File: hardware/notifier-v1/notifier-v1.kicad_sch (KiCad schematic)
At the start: 32 parts, among them J1 USB-C, J2 GC9A01, SW1 RESET, SW2 BOOT, SW3 BUTTON, U1 ESP32-S3-WROOM-1-N8R2, U2 USBLC6-2SC6, U3 AMS1117-3.3, U4 BME688

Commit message: hardware: notifier-v1 rev after design review (buck, sensor peninsula, no via-in-pad)
Review findings applied: TLV62569 buck instead of AMS1117 (0.6 W into the sensor), 500 mA
polyfuse, BME688 on a peninsula with the neck away from the module, custom DRC rule and
KRT settings against vias in SMD pads, signals on the outer layers only, display socket
face past the edge with pin names, more debug pads, antenna strip without pours/vias.
Safe cleanup of router leftovers, one-command pipeline, order checklist.

Co-Authored-By: Claude Opus 5.5 <noreply@anthropic.com>
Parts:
- removed U3: AMS1117-3.3, Package_TO_SOT_SMD:SOT-223-3_TabPin2, symbol Regulator_Linear:AMS1117-3.3
- added F1: 500mA, Fuse:Fuse_1206_3216Metric, symbol Device:Polyfuse
- added L1: 2.2u, Inductor_SMD:L_Cenker_CKCS4030, symbol Device:L
- added R10: 22k, Resistor_SMD:R_0402_1005Metric, symbol Device:R
- added R9: 100k, Resistor_SMD:R_0402_1005Metric, symbol Device:R
- added TP4: 3V3, TestPoint:TestPoint_Pad_D1.0mm, symbol Connector:TestPoint
- added TP5: EN, TestPoint:TestPoint_Pad_D1.0mm, symbol Connector:TestPoint
- added TP6: IO0, TestPoint:TestPoint_Pad_D1.0mm, symbol Connector:TestPoint
- added TP7: VBUS, TestPoint:TestPoint_Pad_D1.0mm, symbol Connector:TestPoint
- added U3: TLV62569, Package_TO_SOT_SMD:SOT-23-5, symbol Regulator_Switching:TLV62569DBV
- R3: value 1k -> 4.7k; LCSC C11702 -> C25900
- TP1, TP2, TP3: footprint TestPoint:TestPoint_Pad_D1.5mm -> TestPoint:TestPoint_Pad_D1.0mm
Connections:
- net +3V3: now also L1.2, R9.1, TP4.1
- net BOOT: now also TP6.1
- net EN: now also TP5.1
- net GND: now also R10.2, U3.2 (GND)
- net VBUS: now also F1.2, TP7.1, U3.1 (EN), U3.4 (VIN); no longer J1.A4 (VBUS), J1.A9 (VBUS), J1.B4 (VBUS), J1.B9 (VBUS), U2.5 (VBUS)
- new net FB: R10.1, R9.2, U3.5 (FB)
- new net SW: L1.1, U3.3 (SW)
- new net VBUS_IN: F1.1, J1.A4 (VBUS), J1.A9 (VBUS), J1.B4 (VBUS), J1.B9 (VBUS), U2.5 (VBUS)

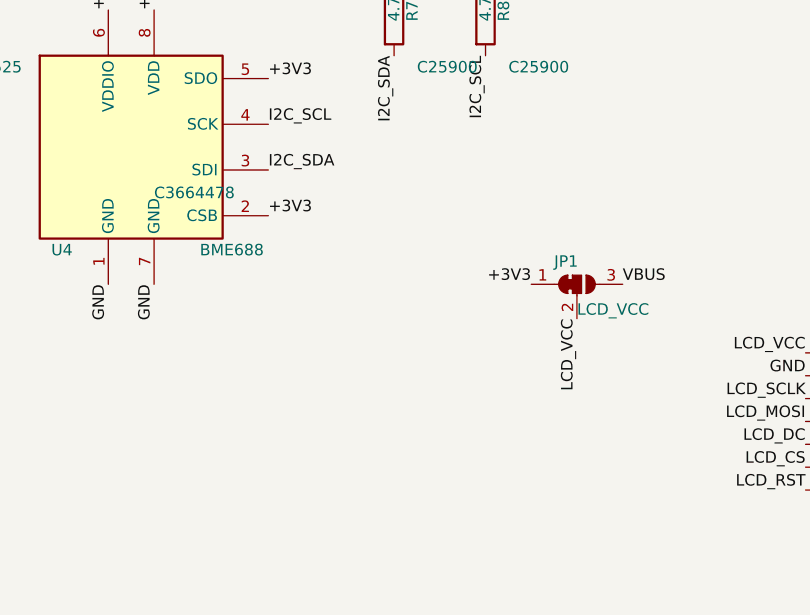
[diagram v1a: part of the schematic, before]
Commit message: hardware: SHT40 for temperature/humidity next to the BME688
The BME688's gas heater warms it, so T/RH come from an SHT40-AD1B (C2909890, 0x44)
in the far corner of the sensor island (about 6 mm away, no pour between them).
The island grows to 11.8 mm with a wider neck; C9->VDD/VSS and SDA/SCL stubs are
hand-drawn because the SHT4x pads are 0.3 mm apart. 3V3/GND track width 0.2 mm
(planes carry the current). finish.py keeps SWIG boards alive between iterations
(an intermittent crash left a dangling via).

Co-Authored-By: Claude Opus 5.5 <noreply@anthropic.com>
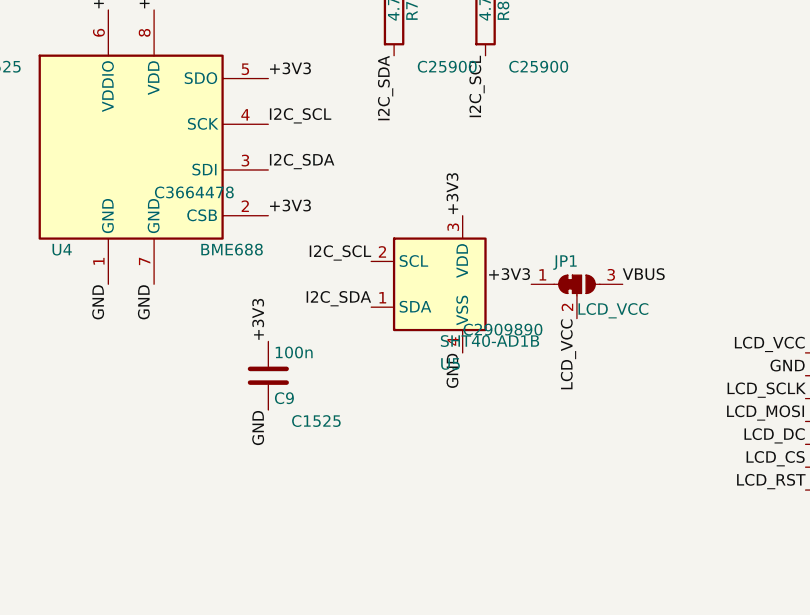
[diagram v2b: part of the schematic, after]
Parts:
- added C9: 100n, Capacitor_SMD:C_0402_1005Metric, symbol Device:C
- added U5: SHT40-AD1B, Sensor_Humidity:Sensirion_DFN-4_1.5x1.5mm_P0.8mm_SHT4x_NoCentralPad, symbol Sensor_Humidity:SHT4x
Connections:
- net +3V3: now also C9.1, U5.3 (VDD)
- net GND: now also C9.2, U5.4 (VSS)
- net I2C_SCL: now also U5.2 (SCL)
- net I2C_SDA: now also U5.1 (SDA)

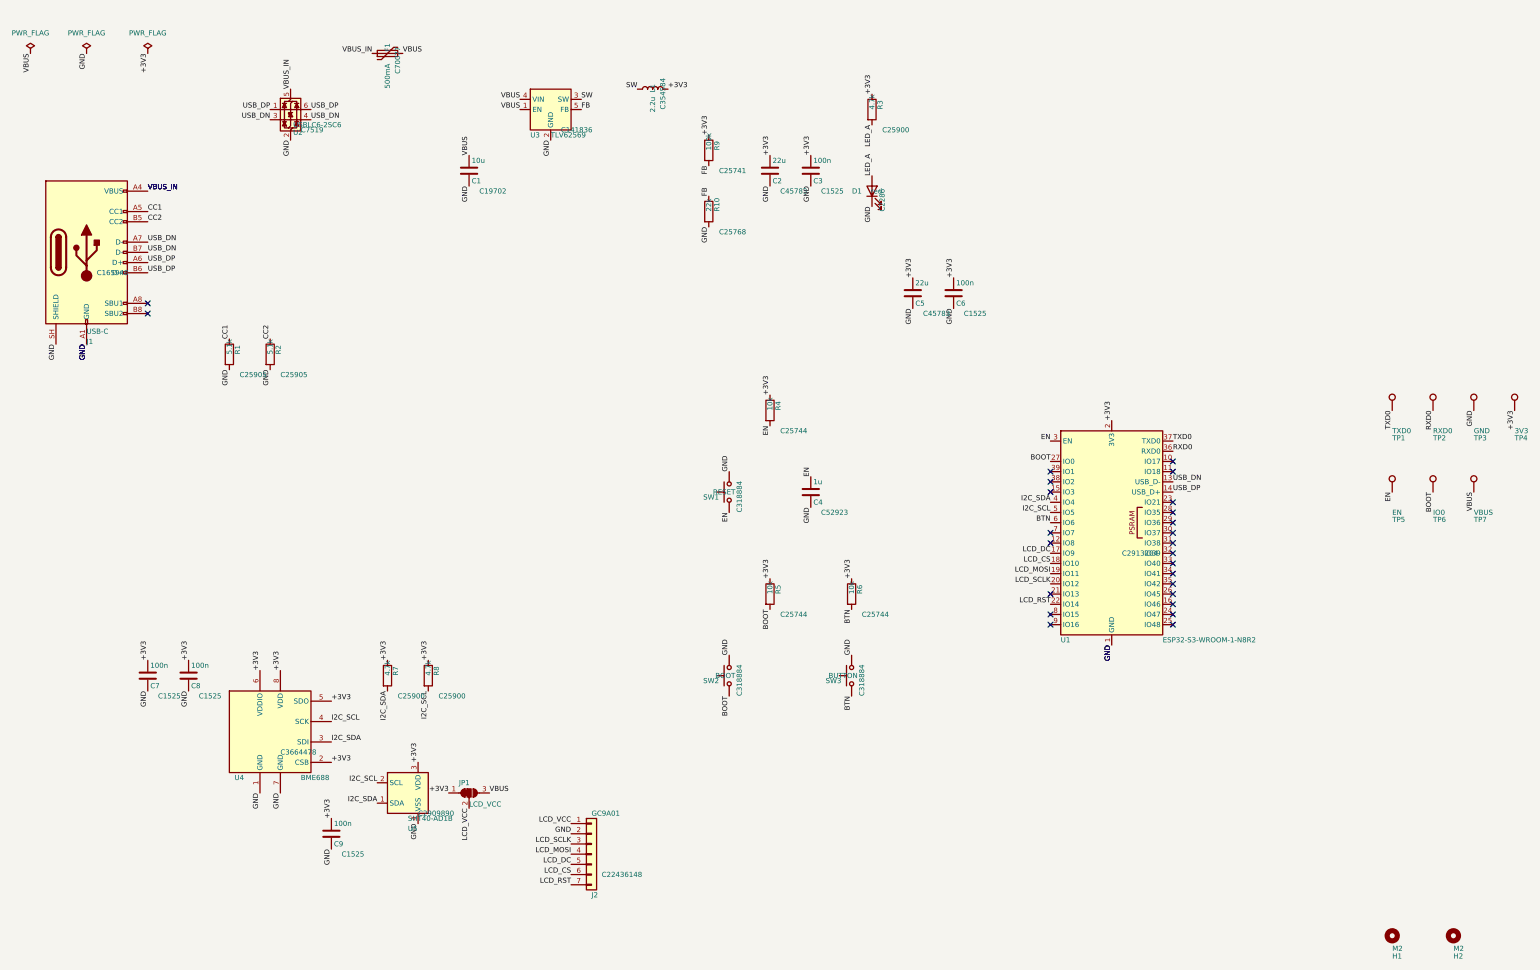
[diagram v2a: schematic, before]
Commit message: Hardware: hierarchical, reviewable schematic (root block diagram + Power, MCU, Sensors, Display)
Real wires for coupled connections, explicit power symbols, notes and title blocks on every sheet.
Power nets are now GND/+3V3/VBUS/VBUS_IN/SW (no leading slash); router and layout patterns updated.

Co-Authored-By: Claude Opus 5.5 <noreply@anthropic.com>
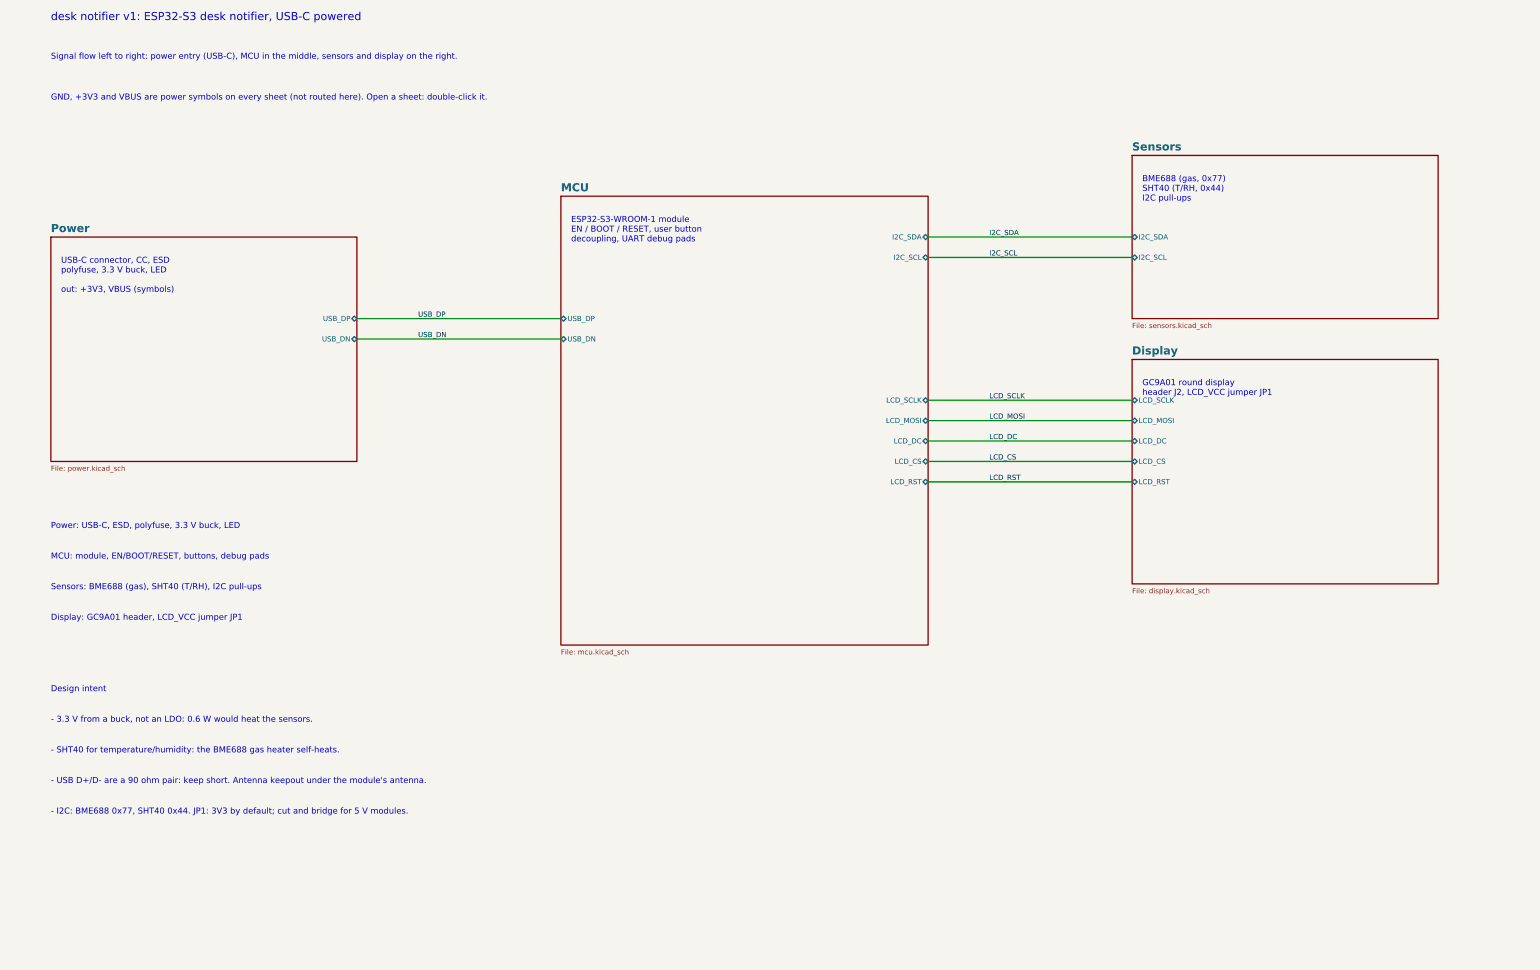
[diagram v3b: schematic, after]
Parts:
- removed C1: 10u, Capacitor_SMD:C_0603_1608Metric, symbol Device:C
- removed C2, C5: 22u, Capacitor_SMD:C_0805_2012Metric, symbol Device:C
- removed C3, C6, C7, C8, C9: 100n, Capacitor_SMD:C_0402_1005Metric, symbol Device:C
- removed C4: 1u, Capacitor_SMD:C_0402_1005Metric, symbol Device:C
- removed D1: red, LED_SMD:LED_0603_1608Metric, symbol Device:LED
- removed F1: 500mA, Fuse:Fuse_1206_3216Metric, symbol Device:Polyfuse
- removed H1, H2: M2, MountingHole:MountingHole_2.2mm_M2, symbol Mechanical:MountingHole
- removed J1: USB-C, Connector_USB:USB_C_Receptacle_HRO_TYPE-C-31-M-12, symbol Connector:USB_C_Receptacle_USB2.0_16P
- removed J2: GC9A01, Connector_PinSocket_2.54mm:PinSocket_1x07_P2.54mm_Horizontal, symbol Connector_Generic:Conn_01x07
- removed JP1: LCD_VCC, Jumper:SolderJumper-3_P1.3mm_Bridged12_RoundedPad1.0x1.5mm, symbol Jumper:SolderJumper_3_Bridged12
- removed L1: 2.2u, Inductor_SMD:L_Cenker_CKCS4030, symbol Device:L
- removed R1, R2: 5.1k, Resistor_SMD:R_0402_1005Metric, symbol Device:R
- removed R10: 22k, Resistor_SMD:R_0402_1005Metric, symbol Device:R
- removed R3, R7, R8: 4.7k, Resistor_SMD:R_0402_1005Metric, symbol Device:R
- removed R4, R5, R6: 10k, Resistor_SMD:R_0402_1005Metric, symbol Device:R
- removed R9: 100k, Resistor_SMD:R_0402_1005Metric, symbol Device:R
- removed SW1: RESET, Button_Switch_SMD:SW_Push_1P1T_XKB_TS-1187A, symbol Switch:SW_Push
- removed SW2: BOOT, Button_Switch_SMD:SW_Push_1P1T_XKB_TS-1187A, symbol Switch:SW_Push
- removed SW3: BUTTON, Button_Switch_SMD:SW_Push_1P1T_XKB_TS-1187A, symbol Switch:SW_Push
- removed TP1: TXD0, TestPoint:TestPoint_Pad_D1.0mm, symbol Connector:TestPoint
- removed TP2: RXD0, TestPoint:TestPoint_Pad_D1.0mm, symbol Connector:TestPoint
- removed TP3: GND, TestPoint:TestPoint_Pad_D1.0mm, symbol Connector:TestPoint
- removed TP4: 3V3, TestPoint:TestPoint_Pad_D1.0mm, symbol Connector:TestPoint
- removed TP5: EN, TestPoint:TestPoint_Pad_D1.0mm, symbol Connector:TestPoint
- removed TP6: IO0, TestPoint:TestPoint_Pad_D1.0mm, symbol Connector:TestPoint
- removed TP7: VBUS, TestPoint:TestPoint_Pad_D1.0mm, symbol Connector:TestPoint
- removed U1: ESP32-S3-WROOM-1-N8R2, RF_Module:ESP32-S3-WROOM-1, symbol RF_Module:ESP32-S3-WROOM-1
- removed U2: USBLC6-2SC6, Package_TO_SOT_SMD:SOT-23-6, symbol Power_Protection:USBLC6-2SC6
- removed U3: TLV62569, Package_TO_SOT_SMD:SOT-23-5, symbol Regulator_Switching:TLV62569DBV
- removed U4: BME688, Package_LGA:Bosch_LGA-8_3x3mm_P0.8mm_ClockwisePinNumbering, symbol Sensor:BME680
- removed U5: SHT40-AD1B, Sensor_Humidity:Sensirion_DFN-4_1.5x1.5mm_P0.8mm_SHT4x_NoCentralPad, symbol Sensor_Humidity:SHT4x
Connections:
- no-connect marks 25 -> 0
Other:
- added sheet Display (display.kicad_sch)
- added sheet MCU (mcu.kicad_sch)
- added sheet Power (power.kicad_sch)
- added sheet Sensors (sensors.kicad_sch)
- note added: "- 3.3 V from a buck, not an LDO: 0.6 W would heat the sensors."
- note added: "- I2C: BME688 0x77, SHT40 0x44. JP1: 3V3 by default; cut and bridge for 5 V modules."
- note added: "- SHT40 for temperature/humidity: the BME688 gas heater self-heats."
- note added: "- USB D+/D- are a 90 ohm pair: keep short. Antenna keepout under the module's antenna."
- note added: "BME688 (gas, 0x77) SHT40 (T/RH, 0x44) I2C pull-ups"
- note added: "Design intent"
- note added: "Display: GC9A01 header, LCD_VCC jumper JP1"
- note added: "ESP32-S3-WROOM-1 module EN / BOOT / RESET, user button decoupling, UART debug pads"
- note added: "GC9A01 round display header J2, LCD_VCC jumper JP1"
- note added: "GND, +3V3 and VBUS are power symbols on every sheet (not routed here). Open a sheet: double-click it."
- note added: "MCU: module, EN/BOOT/RESET, buttons, debug pads"
- note added: "Power: USB-C, ESD, polyfuse, 3.3 V buck, LED"
- note added: "Sensors: BME688 (gas), SHT40 (T/RH), I2C pull-ups"
- note added: "Signal flow left to right: power entry (USB-C), MCU in the middle, sensors and display on the right."
- note added: "USB-C connector, CC, ESD polyfuse, 3.3 V buck, LED out: +3V3, VBUS (symbols)"
- note added: "desk notifier v1: ESP32-S3 desk notifier, USB-C powered"
